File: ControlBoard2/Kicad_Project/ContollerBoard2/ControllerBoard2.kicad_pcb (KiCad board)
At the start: 2 copper layers, 26.2 x 43.2 mm, 34 parts, among them J1 Main Header, J2 SWD, J3 WD_Disable, Q1 BSS84, U1 STM32F303K8Tx, U2 UJA1075A-3.3, Y1 8Mhz

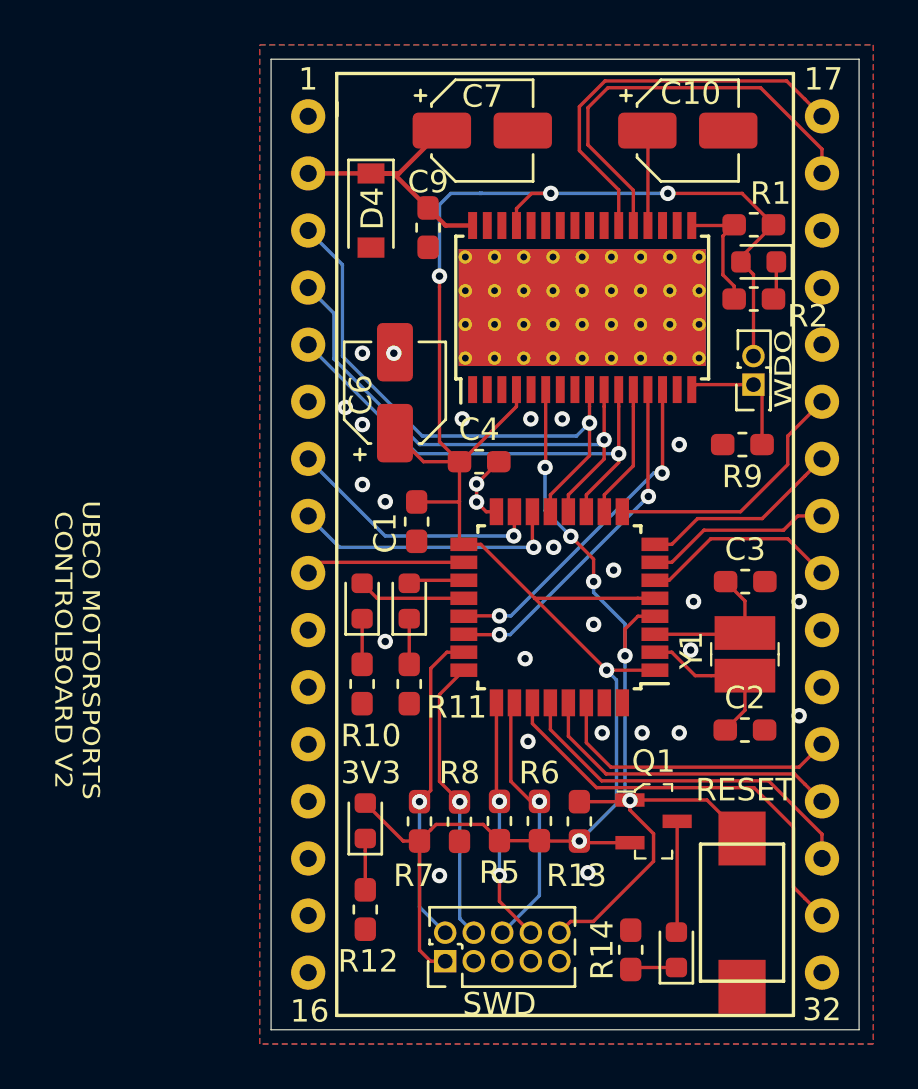
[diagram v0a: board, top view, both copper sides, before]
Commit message: Improved routing and generated BOM
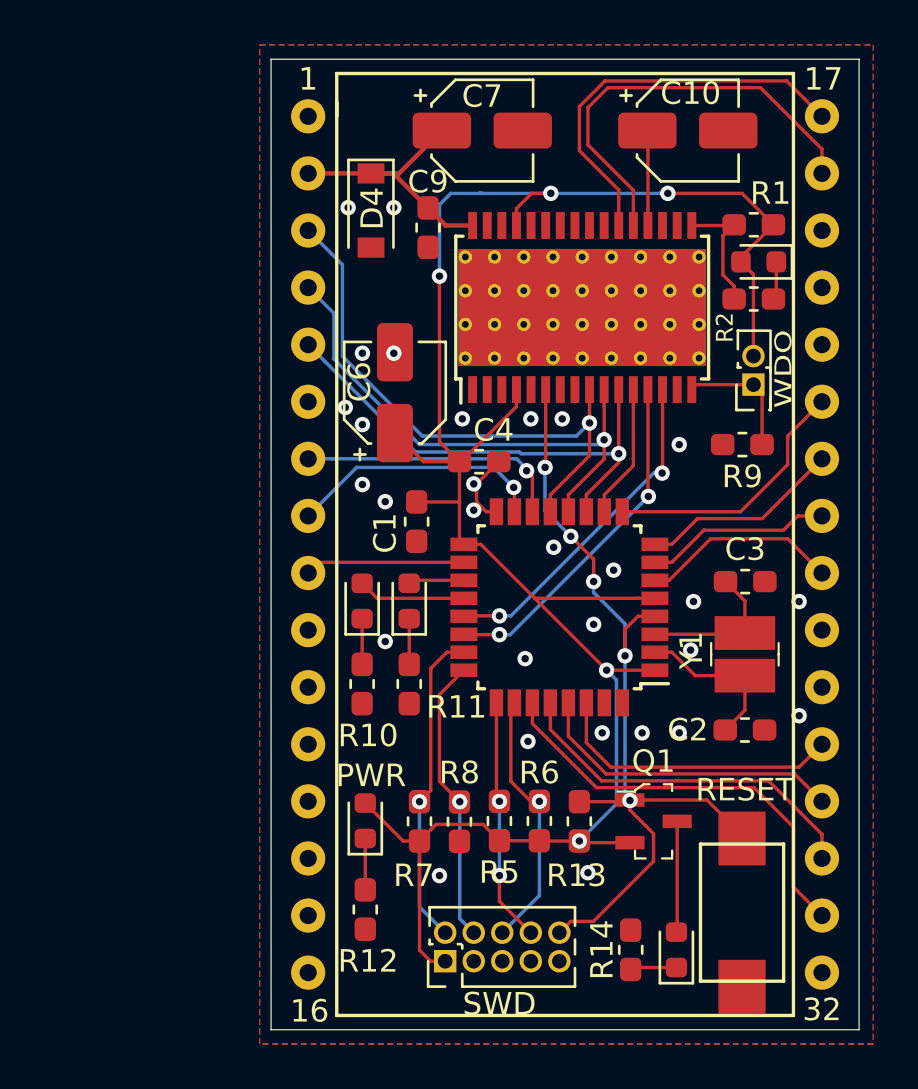
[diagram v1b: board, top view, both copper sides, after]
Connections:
- J1 pad 7: (no net) -> PB0
- J1 pad 8: (no net) -> PB1
- U1 pad 14: (no net) -> PB0
- U1 pad 15: (no net) -> PB1
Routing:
- net (no net): track 38.3 -> 14.4 mm, vias 2 -> 0
- net PB0: track 0.00 -> 11.9 mm, vias 0 -> 1
- net PB1: track 0.00 -> 11.5 mm, vias 0 -> 1
- net GND: vias 27 -> 29
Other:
- board text added: "LV 10/2020"
- board text added: "PWR"
- board text removed: "3V3"
- board text removed: "LV 1/2020"

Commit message: Finished MainBoard. Small routing improvements on ControlBoard
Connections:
- D2 pad 2: (no net) -> PA10
- D3 pad 2: (no net) -> PA9
- J1 pad 20: (no net) -> +3V3
- J1 pad 9: (no net) -> PA8
- U1 pad 18: (no net) -> PA8
- U1 pad 19: (no net) -> PA9
- U1 pad 20: (no net) -> PA10
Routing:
- net (no net): track 14.4 -> 0.00 mm
- net PA8: track 0.00 -> 7.12 mm
- net PA10: track 0.00 -> 4.88 mm
- net GND: track 3.27 -> 7.83 mm, vias 29 -> 28
- net +3V3: track 94.1 -> 96.7 mm
- net PA9: track 0.00 -> 2.49 mm
- net PA3: track 11.7 -> 12.6 mm
- net CAN_RX: track 15.2 -> 14.7 mm
